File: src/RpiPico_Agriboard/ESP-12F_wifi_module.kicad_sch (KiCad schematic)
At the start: 12 parts, among them J27 Conn_02x05_Odd_Even, SW3 SW_Push, SW4 SW_Push, U4 ESP-12F

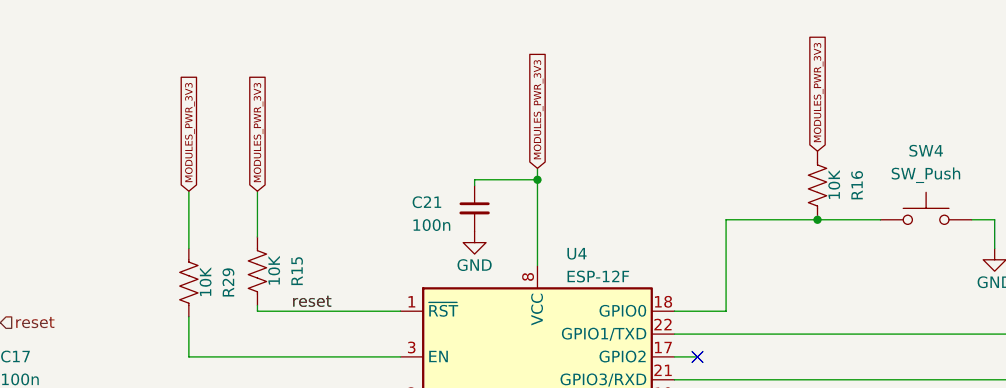
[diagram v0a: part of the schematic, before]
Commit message: layut updates, 3v3 sensor pwr updates
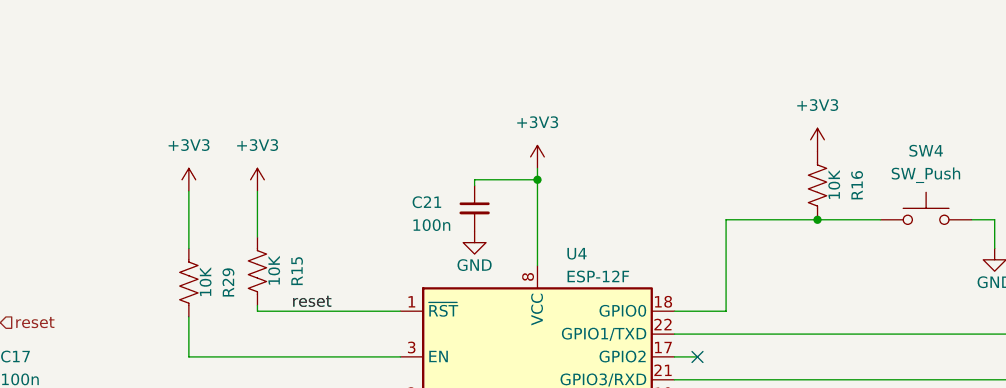
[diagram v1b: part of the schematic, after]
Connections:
- net MODULES_PWR_3V3 is gone; now on net +3V3: C21.1, R15.1, R16.1, R29.1, U4.8 (VCC)
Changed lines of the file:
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@@
     (effects (font (size 1.27 1.27)) (justify left bottom))
-  )
-  (global_label "MODULES_PWR_3V3" (shape input) (at 100.965 52.705 90) (fields_autoplaced)
-    (effects (font (size 0.8 0.8)) (justify left))
-    (property "Intersheetrefs" "${INTERSHEET_REFS}" (at 100.965 39.4081 90)
-      (effects (font (size 1.27 1.27)) (justify left) hide)
-    )
-  )
-  (global_label "MODULES_PWR_3V3" (shape input) (at 170.815 48.26 90) (fields_autoplaced)
-    (effects (font (size 0.8 0.8)) (justify left))
-    (property "Intersheetrefs" "${INTERSHEET_REFS}" (at 170.815 34.9631 90)
-      (effects (font (size 1.27 1.27)) (justify left) hide)
-    )
-  )
-  (global_label "MODULES_PWR_3V3" (shape input) (at 139.7 50.165 90) (fields_autoplaced)
-    (effects (font (size 0.8 0.8)) (justify left))
-    (property "Intersheetrefs" "${INTERSHEET_REFS}" (at 139.7 36.8681 90)
-      (effects (font (size 1.27 1.27)) (justify left) hide)
-    )
-  )
-  (global_label "MODULES_PWR_3V3" (shape input) (at 108.585 52.705 90) (fields_autoplaced)
-    (effects (font (size 0.8 0.8)) (justify left))
-    (property "Intersheetrefs" "${INTERSHEET_REFS}" (at 108.585 39.4081 90)
-      (effects (font (size 1.27 1.27)) (justify left) hide)
-    )
   )
   (hierarchical_label "ESP8266_RX_out" (shape input) (at 217.17 106.045 0) (fields_autoplaced)
@@
     )
   )
+  (symbol (lib_id "power:+3V3") (at 170.815 48.26 0) (unit 1)
+    (in_bom yes) (on_board yes) (dnp no) (fields_autoplaced)
+    (property "Reference" "#PWR024" (at 170.815 52.07 0)
+      (effects (font (size 1.27 1.27)) hide)
+    )
+    (property "Value" "+3V3" (at 170.815 43.18 0)
+      (effects (font (size 1.27 1.27)))
+    )
+    (property "Footprint" "" (at 170.815 48.26 0)
+      (effects (font (size 1.27 1.27)) hide)
+    )
+    (property "Datasheet" "" (at 170.815 48.26 0)
+      (effects (font (size 1.27 1.27)) hide)
+    )
+    (pin "1")
+    (instances
+      (project "RpiPico_Agriboard"
+        (path "/c2474b65-c0e8-4987-86b2-fddddd4113dc/24a6f6dd-59ed-4a3f-ab3f-0a381255370f"
+          (reference "#PWR024") (unit 1)
+        )
+        (path "/c2474b65-c0e8-4987-86b2-fddddd4113dc/24a6f6dd-59ed-4a3f-ab3f-0a381255370f/72a22278-332d-4fac-9f87-e146604ac9df"
+          (reference "#PWR0105") (unit 1)
+        )
+      )
+    )
+  )
   (symbol (lib_id "power:GND") (at 186.69 108.585 0) (unit 1)
     (in_bom yes) (on_board yes) (dnp no)
@@
     )
   )
+  (symbol (lib_id "power:+3V3") (at 100.965 52.705 0) (unit 1)
+    (in_bom yes) (on_board yes) (dnp no) (fields_autoplaced)
+    (property "Reference" "#PWR024" (at 100.965 56.515 0)
+      (effects (font (size 1.27 1.27)) hide)
+    )
+    (property "Value" "+3V3" (at 100.965 47.625 0)
+      (effects (font (size 1.27 1.27)))
+    )
+    (property "Footprint" "" (at 100.965 52.705 0)
+      (effects (font (size 1.27 1.27)) hide)
+    )
+    (property "Datasheet" "" (at 100.965 52.705 0)
+      (effects (font (size 1.27 1.27)) hide)
+    )
+    (pin "1")
+    (instances
+      (project "RpiPico_Agriboard"
+        (path "/c2474b65-c0e8-4987-86b2-fddddd4113dc/24a6f6dd-59ed-4a3f-ab3f-0a381255370f"
+          (reference "#PWR024") (unit 1)
+        )
+        (path "/c2474b65-c0e8-4987-86b2-fddddd4113dc/24a6f6dd-59ed-4a3f-ab3f-0a381255370f/72a22278-332d-4fac-9f87-e146604ac9df"
+          (reference "#PWR072") (unit 1)
+        )
+      )
+    )
+  )
   (symbol (lib_id "power:GND") (at 132.715 57.15 0) (unit 1)
     (in_bom yes) (on_board yes) (dnp no)
@@
         )
       )
+    )
+  )
+  (symbol (lib_id "power:+3V3") (at 108.585 52.705 0) (unit 1)
+    (in_bom yes) (on_board yes) (dnp no) (fields_autoplaced)
+    (property "Reference" "#PWR024" (at 108.585 56.515 0)
+      (effects (font (size 1.27 1.27)) hide)
+    )
+    (property "Value" "+3V3" (at 108.585 47.625 0)
+      (effects (font (size 1.27 1.27)))
+    )
+    (property "Footprint" "" (at 108.585 52.705 0)
+      (effects (font (size 1.27 1.27)) hide)
+    )
+    (property "Datasheet" "" (at 108.585 52.705 0)
+      (effects (font (size 1.27 1.27)) hide)
+    )
+    (pin "1")
+    (instances
+      (project "RpiPico_Agriboard"
+        (path "/c2474b65-c0e8-4987-86b2-fddddd4113dc/24a6f6dd-59ed-4a3f-ab3f-0a381255370f"
+          (reference "#PWR024") (unit 1)
+        )
+        (path "/c2474b65-c0e8-4987-86b2-fddddd4113dc/24a6f6dd-59ed-4a3f-ab3f-0a381255370f/72a22278-332d-4fac-9f87-e146604ac9df"
+          (reference "#PWR073") (unit 1)
+        )
+      )
+    )
+  )
+  (symbol (lib_id "power:+3V3") (at 139.7 50.165 0) (unit 1)
+    (in_bom yes) (on_board yes) (dnp no) (fields_autoplaced)
+    (property "Reference" "#PWR024" (at 139.7 53.975 0)
+      (effects (font (size 1.27 1.27)) hide)
+    )
+    (property "Value" "+3V3" (at 139.7 45.085 0)
+      (effects (font (size 1.27 1.27)))
+    )
+    (property "Footprint" "" (at 139.7 50.165 0)
+      (effects (font (size 1.27 1.27)) hide)
+    )
+    (property "Datasheet" "" (at 139.7 50.165 0)
+      (effects (font (size 1.27 1.27)) hide)
+    )
+    (pin "1")
+    (instances
+      (project "RpiPico_Agriboard"
+        (path "/c2474b65-c0e8-4987-86b2-fddddd4113dc/24a6f6dd-59ed-4a3f-ab3f-0a381255370f"
+          (reference "#PWR024") (unit 1)
+        )
+        (path "/c2474b65-c0e8-4987-86b2-fddddd4113dc/24a6f6dd-59ed-4a3f-ab3f-0a381255370f/72a22278-332d-4fac-9f87-e146604ac9df"
+          (reference "#PWR097") (unit 1)
+        )
+      )

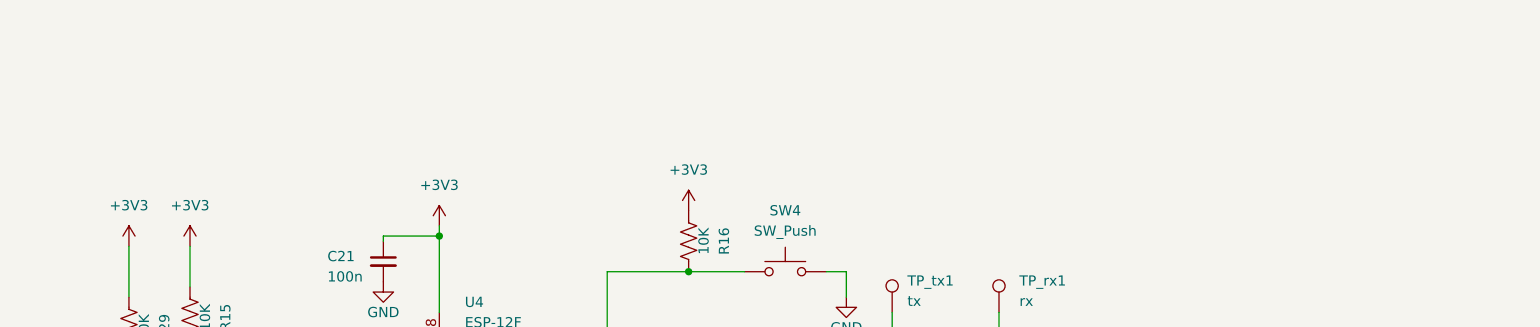
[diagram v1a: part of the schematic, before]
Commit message: complete board update and routing
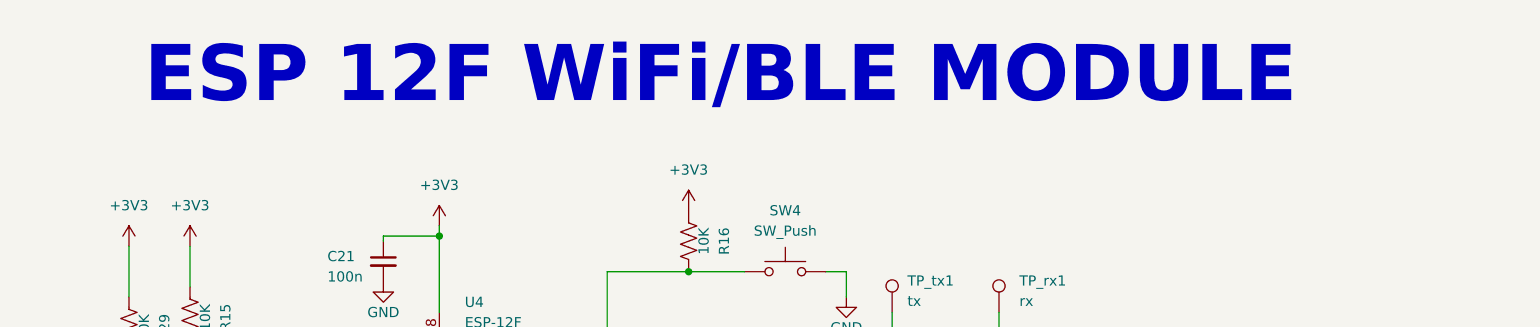
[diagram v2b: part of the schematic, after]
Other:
- note added: "ESP 12F WiFi/BLE MODULE"
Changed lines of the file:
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@@
     (stroke (width 0) (type default))
+  )
+  (text "ESP 12F WiFi/BLE MODULE" (at 102.87 35.56 0)
+    (effects (font (face "Agency FB") (size 7 7) bold) (justify left bottom))
   )
   (label "ESP8266_TX" (at 216.535 68.58 0) (fields_autoplaced)
